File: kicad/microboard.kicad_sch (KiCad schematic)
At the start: 11 parts, among them J2 Microboard, J3 Microboard, U2 DRV5011ADDBZR, U3 HT7550, U5 LM35-LP

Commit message: [webpage] use h3 for assembly link
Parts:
- J3: value Microboard -> Baseboard
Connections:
- net +3.3V: now also J2.3 (Pin_3), J3.3 (Pin_3); no longer J2.2 (Pin_2), J3.4 (Pin_4)
- net GND: now also J2.2 (Pin_2); no longer J2.5 (Pin_5)
- net Hall: now also J2.5 (Pin_5); no longer J2.4 (Pin_4)
- net ThermAnalog: now also J2.4 (Pin_4), J3.4 (Pin_4); no longer J2.3 (Pin_3), J3.3 (Pin_3)
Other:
- moved on the sheet: J2

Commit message: v1.5.1
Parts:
- removed C18: 1u, Capacitor_SMD:C_0805_2012Metric_Pad1.18x1.45mm_HandSolder, symbol Device:C
- removed C19: .01u, Capacitor_SMD:C_0805_2012Metric_Pad1.18x1.45mm_HandSolder, symbol Device:C
- removed C2, C5: 10u, Capacitor_SMD:C_0805_2012Metric_Pad1.18x1.45mm_HandSolder, symbol Device:C
- removed C20: .01u, dank:CAP_3216_TDK, symbol dank:CGA5L2NP01H104J160AA
- removed U2: DRV5011ADDBZR, dank:DBZ0003A_L, symbol dank:DRV5011ADDBZR
- added C17, C20: .01u, dank:CAP_CL_21_SAM, symbol dank:CL21C103JBF1PNE
- added C19: 1u, dank:CAPC230145_140N_KEM, symbol dank:C0805C105J3RECAUTO
- added C2, C5: 10u, dank:CAP_CL21B106KOQNNNE_SAM, symbol dank:CL21B106KOQNNNE
- added R20: 10k, PCM_Resistor_SMD_AKL:R_0805_2012Metric_Pad1.15x1.40mm_HandSolder, symbol Device:R
- added U2: AH3712Q-P-B, dank:TRANS_AH3712-P-B_DIO, symbol dank:AH3712Q-P-B
- J2: value Microboard -> to microboard
- J3: value Baseboard -> to baseboard
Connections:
- net +12V: no longer J3.1 (Pin_1), U3.2 (VIN)
- net +3.3V: no longer J3.3 (Pin_3)
- net +5VA: now also C20.1, C5.2
- net GND: now also C17.2, C19.2, C2.2, C20.2, C5.1, U2.2 (GND)
- net Hall: no longer J3.5 (Pin_5)
- net ThermAnalog: no longer J3.4 (Pin_4), R21.1, U5.2 (V_{OUT})
- net at R21.2: now also C19.1
- new net +12Vmicro: C2.1, J3.1 (Pin_1), U3.2 (VIN)
- new net +3.3Vmicro: C17.1, J3.3 (Pin_3), R20.2, U2.1 (VDD)
- new net HallMicro: J3.5 (Pin_5), R20.1, U2.3 (OUTPUT)
- new net ThermMicro: J3.4 (Pin_4), R21.1, U5.2 (V_{OUT})
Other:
- note added: "3-27V, 4.8mA, max out 60mA@VDD±0.3 (0.165W), operational to 150C."
- note added: "Through-holes poke through the ceiling of the cool chamber, and are soldered to the board. Another battery of screw terminals exchanges five wires with the mainboard. This allows us to keep our capacitors near the devices, where we want them (though not as close as if we were using SMT components)."
- note removed: "2.5-5.5V, 3mA, max out 30mA@VDD±0.3 (0.159W), operational to 135C."
- note removed: "Through-holes poke through the ceiling of the cool chamber, and are soldered to the board. Another battery of screw terminals exchanges five wires with the mainboard. This allows us to keep our capacitors near the devices, where we want them (though not as close as on the SMT version of the board)."

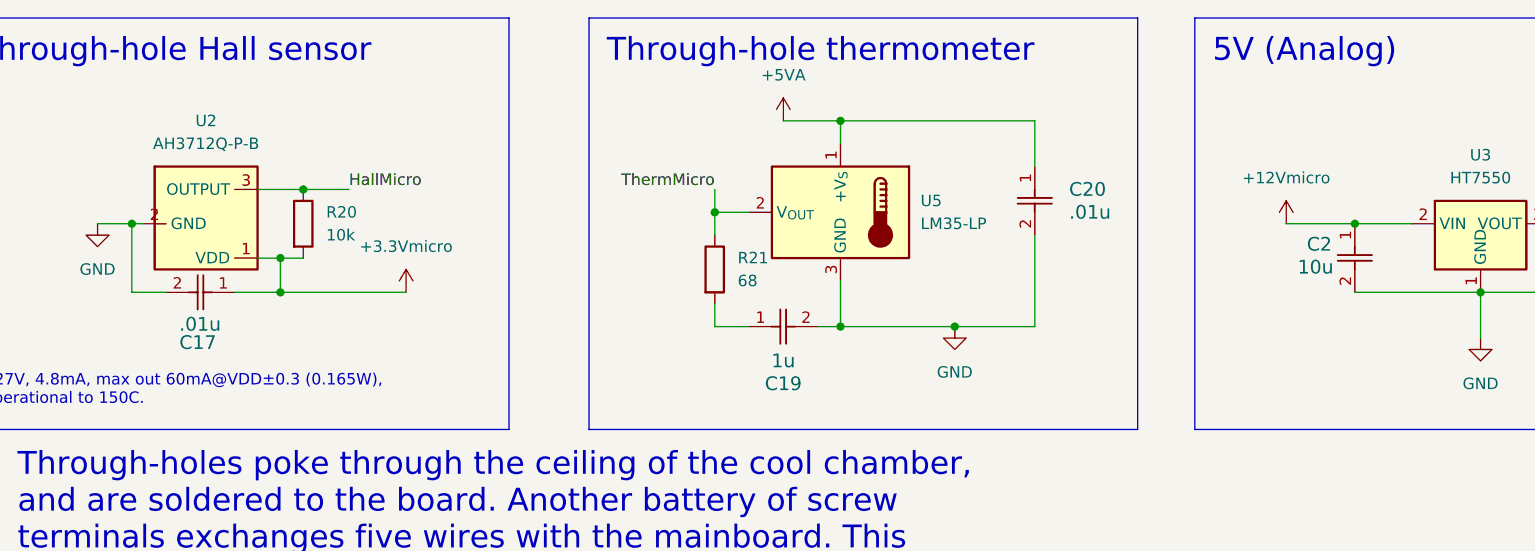
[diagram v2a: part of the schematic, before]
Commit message: update to 1206 where appropriate
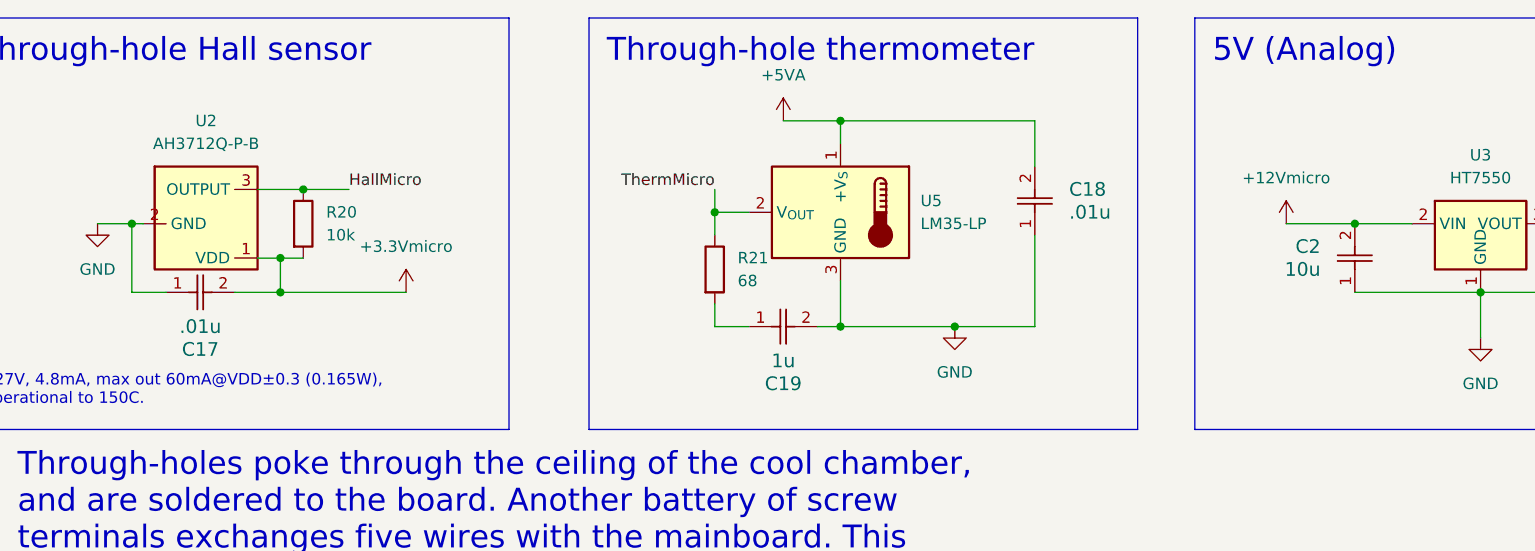
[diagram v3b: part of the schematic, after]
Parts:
- removed C17, C20: .01u, dank:CAP_CL_21_SAM, symbol dank:CL21C103JBF1PNE
- removed C19: 1u, dank:CAPC230145_140N_KEM, symbol dank:C0805C105J3RECAUTO
- removed C2, C5: 10u, dank:CAP_CL21B106KOQNNNE_SAM, symbol dank:CL21B106KOQNNNE
- added C17, C18: .01u, dank:CAP_CL31_SAM, symbol dank:CL31B103KHFNFNE
- added C19: 1u, dank:CAP_CL31_SAM, symbol dank:CL31B105KAHNNNE
- added C2, C5: 10u, dank:CAP_CL31_SAM, symbol dank:CL31B106KAHNNNE
- R20, R21: footprint PCM_Resistor_SMD_AKL:R_0805_2012Metric_Pad1.15x1.40mm_HandSolder -> PCM_Resistor_SMD_AKL:R_1206_3216Metric_Pad1.30x1.75mm_HandSolder
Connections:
- net +12Vmicro: now also C2.2
- net +3.3Vmicro: now also C17.2
- net +5VA: now also C18.2, C5.2
- net GND: now also C17.1, C18.1, C19.2, C2.1, C5.1
- net at R21.2: now also C19.1

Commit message: v1.7.0 upgrade most C/R to 1206 from 0805
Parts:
- added J12: testpin, Connector_PinHeader_1.00mm:PinHeader_1x01_P1.00mm_Vertical, symbol Connector:Conn_01x01_Pin
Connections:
- net +5VA: now also J12.1 (Pin_1)
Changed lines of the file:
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@@
 	(title_block
 		(title "dankdryer")
-		(date "2025-02-16")
-		(rev "1.6.0")
+		(date "2025-02-18")
+		(rev "1.7.0")
 		(company "dirty south supercomputing")
 		(comment 1 "nick black")
@@
 	)
 	(junction
+		(at 229.87 76.2)
+		(diameter 0)
+		(color 0 0 0 0)
+	)
+	(junction
 		(at 71.12 140.97)
 		(diameter 0)
@@
 	(wire
 		(pts
-			(xy 218.44 76.2) (xy 232.41 76.2)
+			(xy 218.44 76.2) (xy 229.87 76.2)
 		)
 		(stroke
@@
 		(pts
 			(xy 71.12 140.97) (xy 71.12 139.7)
+		)
+		(stroke
+			(width 0)
+			(type default)
+		)
+	)
+	(wire
+		(pts
+			(xy 229.87 76.2) (xy 232.41 76.2)
 		)
 		(stroke
@@
 					(unit 1)
 				)
+			)
+		)
+	)
+	(symbol
+		(lib_id "Connector:Conn_01x01_Pin")
+		(at 229.87 81.28 90)
+		(unit 1)
+		(exclude_from_sim no)
+		(in_bom yes)
+		(on_board yes)
+		(dnp no)
+		(fields_autoplaced yes)
+		(property "Reference" "J12"
+			(at 231.14 79.3749 90)
+			(effects
+				(font
+					(size 1.27 1.27)
+				)
+				(justify right)
+			)
+		)
+		(property "Value" "testpin"
+			(at 231.14 81.9149 90)
+			(effects
+				(font
+					(size 1.27 1.27)
+				)
+				(justify right)
+			)
+		)
+		(property "Footprint" "Connector_PinHeader_1.00mm:PinHeader_1x01_P1.00mm_Vertical"
+			(at 229.87 81.28 0)
+			(effects
+				(font
+					(size 1.27 1.27)
+				)
+				(hide yes)
+			)
+		)
+		(property "Datasheet" "~"
+			(at 229.87 81.28 0)
+			(effects
+				(font
+					(size 1.27 1.27)
+				)
+				(hide yes)
+			)
+		)
+		(property "Description" "Generic connector, single row, 01x01, script generated"
+			(at 229.87 81.28 0)
+			(effects
+				(font
+					(size 1.27 1.27)
+				)
+				(hide yes)
+			)
+		)
+		(pin "1"
+		)
+		(instances
+			(project "dankdryer"
+				(path "/0e28ce9c-097a-4614-9b8c-9333a7b96611/e87156ca-67c4-4a67-9b05-7ba1374951ea"
+					(reference "J12")
+					(unit 1)
+				)

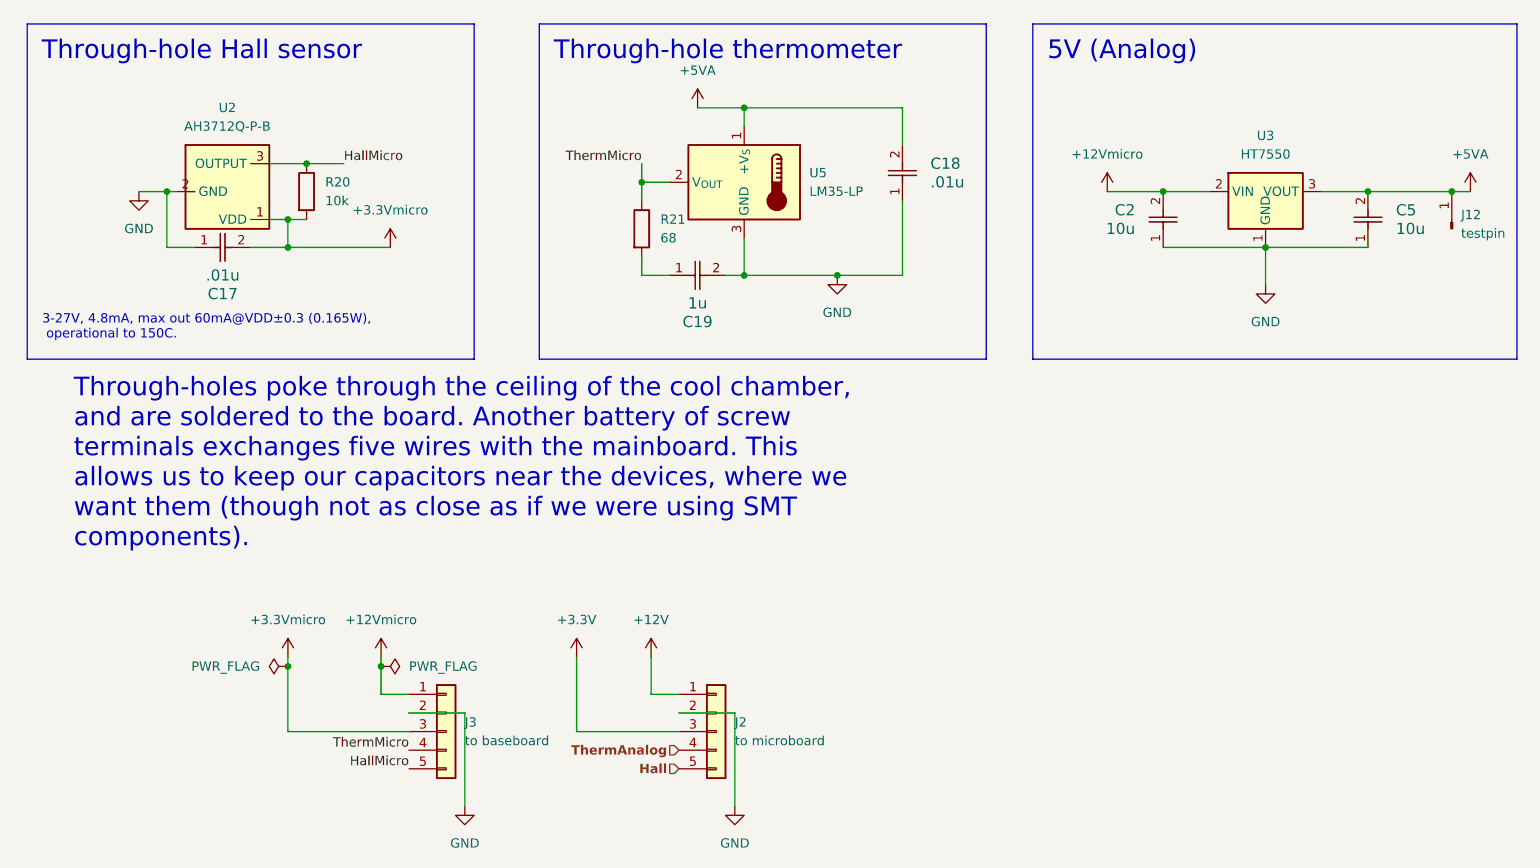
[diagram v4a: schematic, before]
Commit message: 1.7.2: move fan capacitors to 1206
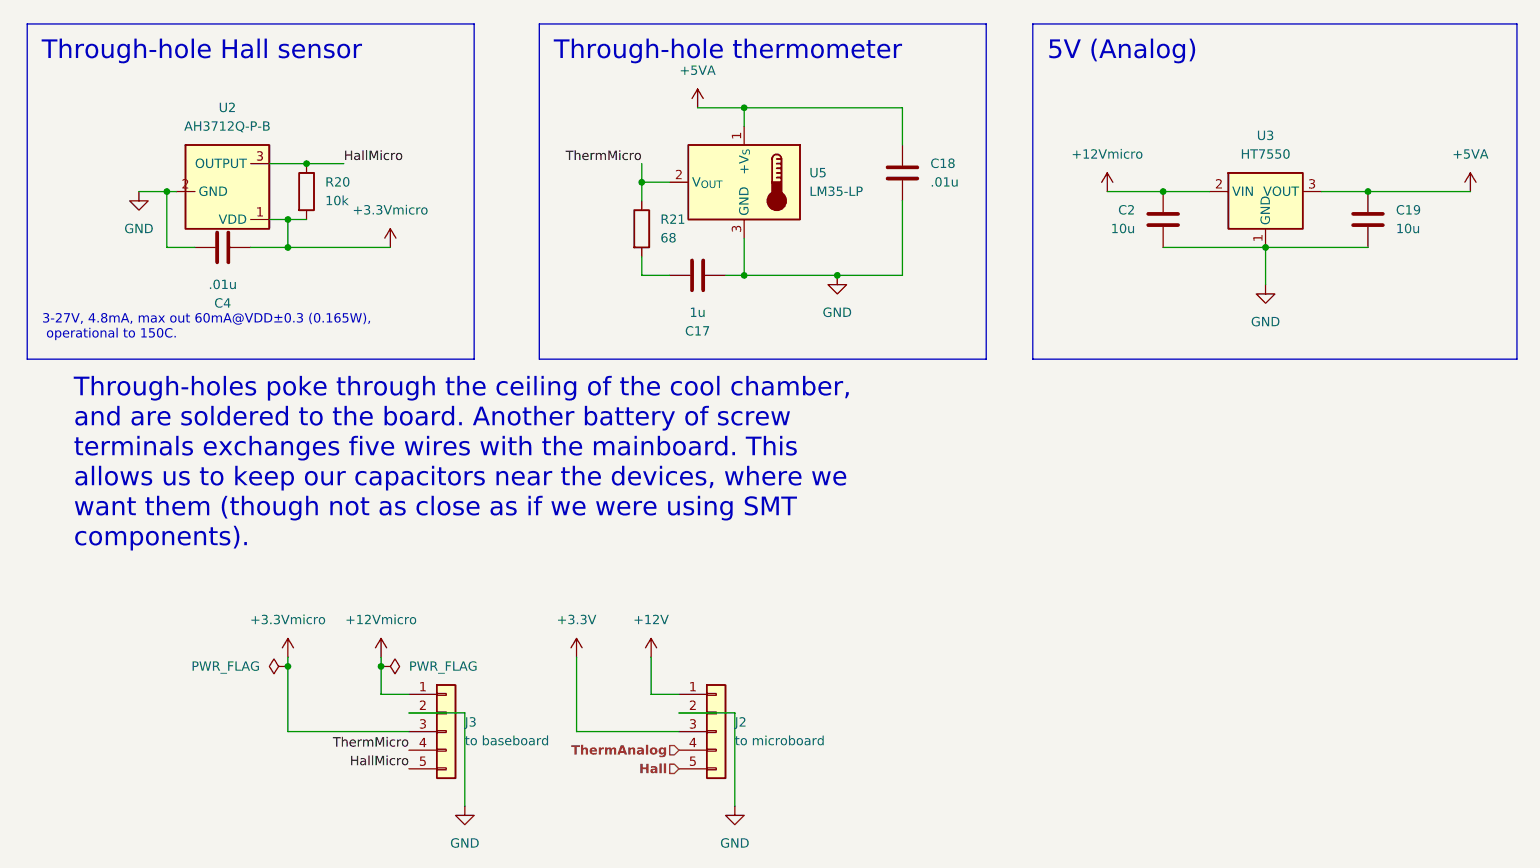
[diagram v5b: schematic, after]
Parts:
- removed C17, C18: .01u, dank:CAP_CL31_SAM, symbol dank:CL31B103KHFNFNE
- removed C19: 1u, dank:CAP_CL31_SAM, symbol dank:CL31B105KAHNNNE
- removed C2, C5: 10u, dank:CAP_CL31_SAM, symbol dank:CL31B106KAHNNNE
- removed J12: testpin, Connector_PinHeader_1.00mm:PinHeader_1x01_P1.00mm_Vertical, symbol Connector:Conn_01x01_Pin
- added C17: 1u, Capacitor_SMD:C_1206_3216Metric_Pad1.33x1.80mm_HandSolder, symbol Device:C
- added C18, C4: .01u, Capacitor_SMD:C_1206_3216Metric_Pad1.33x1.80mm_HandSolder, symbol Device:C
- added C19, C2: 10u, Capacitor_SMD:C_1206_3216Metric_Pad1.33x1.80mm_HandSolder, symbol Device:C
- R20, R21: footprint PCM_Resistor_SMD_AKL:R_1206_3216Metric_Pad1.30x1.75mm_HandSolder -> Resistor_SMD:R_1206_3216Metric_Pad1.30x1.75mm_HandSolder
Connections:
- net +12Vmicro: now also C2.1
- net +3.3Vmicro: now also C4.2
- net +5VA: now also C18.1, C19.1
- net GND: now also C17.2, C18.2, C19.2, C2.2, C4.1
- net at R21.2: now also C17.1

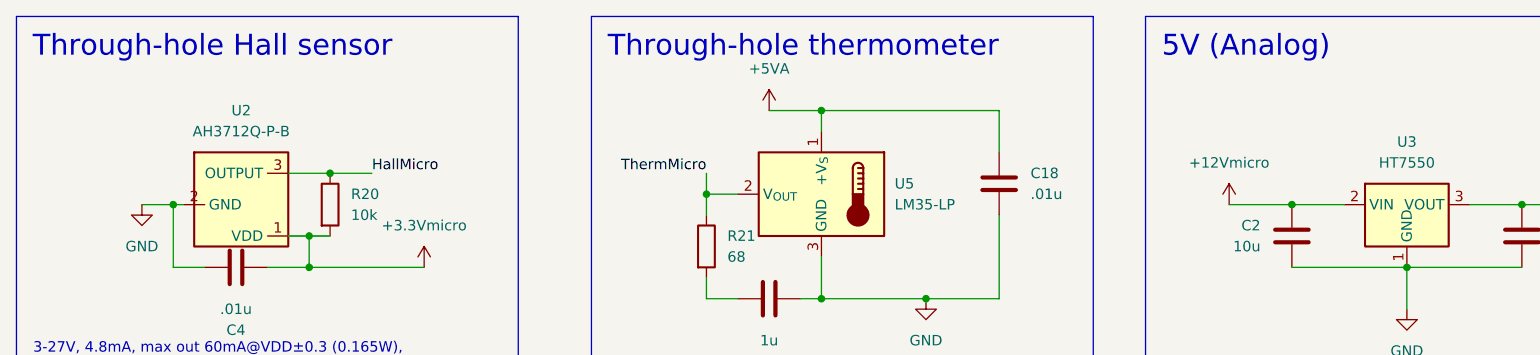
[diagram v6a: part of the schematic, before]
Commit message: upgrade to kicad9
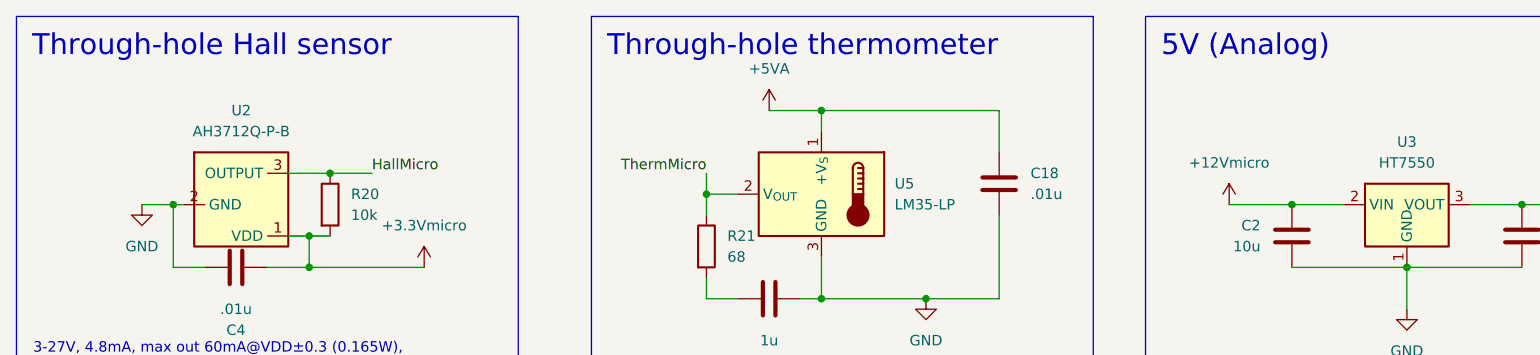
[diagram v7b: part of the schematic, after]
